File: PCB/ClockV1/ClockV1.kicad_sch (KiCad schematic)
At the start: 41 parts, among them J1 Conn_01x02, J2 Conn_01x02, J3 Conn_01x08, J4 Conn_01x02, Q1 FDN327N, Q2 DMP2045UQ-7, U1 MT3608, U2 MAX14611ETD_, U3 DFR0299, U4 ATtiny1616-M

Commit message: Production to JLCPCB
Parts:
- added H5, H6, H7: MountingHole, MountingHole:ToolingHole_1.152mm, symbol Mechanical:MountingHole
- D2: value BAT43 -> LBAT46T1G
- D3: value LED -> Red; now left out of the parts list
- D4: value LED -> Green; now left out of the parts list
- J1, J2, J3, J4, R6, TP1, TP2, TP3, TP4, TP5, TP6, TP7, U3: now left out of the parts list
- L1: JLCPCB Part # (none) -> C5123081; MANUFACTURER_PART_NUMBER (none) -> SDRH.1209CT.NLF220MT00
- Q2: value DMP2045UQ-7 -> AO3407A; footprint Samacsys:SOT96P240X110-3N -> Package_TO_SOT_SMD:SOT-23-3; Arrow Part Number DMP2045UQ-7 -> (none); Arrow Price/Stock https://www.arrow.com/en/products/dmp2045uq-7/diodes-incorp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 -> (none); JLCPCB Part # (none) -> C5224209; Manufacturer_Name Diodes Incorporated -> ElecSuper; Manufacturer_Part_Number DMP2045UQ-7 -> AO3407A; Mouser Part Number 621-DMP2045UQ-7 -> (none); Mouser Price/Stock https://www.mouser.co.uk/ProductDetail/Diodes-Incorporated/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 -> (none)
- R2: value 442k -> 330k
- U2: value MAX14611ETD_ -> MAX14611ETD+T; JLCPCB Part # (none) -> C2677488

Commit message: Add decoupling capacitors and signal selection jumper for MAX14611
- Added decoupling capacitors (C5/100nF and C6/1uF) for the MAX14611 dual power supplies
- Added solder jumper to allow selection between PON and BR signals for microcontroller input
- Renamed net HBR to Net-(JP2-C) to better reflect its function as jumper connection
- Added new HPONBR signal net for level shifter power control
- Updated PCB date to 2025-05-11
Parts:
- added C5: 100nF, Capacitor_SMD:C_0603_1608Metric, symbol Device:C
- added C6: 1uF, Capacitor_SMD:C_0603_1608Metric, symbol Device:C
- added JP2: PON/BR Select, Jumper:SolderJumper-3_P1.3mm_Open_RoundedPad1.0x1.5mm, symbol Jumper:Jumper_3_Open
- TP2: value HBR -> HPONBR
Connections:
- net +1V5: now also C5.1
- net +3V3: now also C6.1
- net BR: now also JP2.1 (A); no longer U2.2 (I/OVL2)
- net GND: now also C5.2, C6.2
- net PON: now also JP2.3 (B)
- net HBR renamed HPONBR
- new net: JP2.2 (C), U2.2 (I/OVL2)
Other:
- moved on the sheet: JP1, TP1, TP2, TP3, TP4, U2

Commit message: Update of PCB ClockV1
- Export Silkscreen in 3D
- Add jumper to select monitoring PON
- Re-order references
- Monitor +3V0 from uC with ADC and a decoupling capactior
- Changed photoresistor footprint (actual part is smaller than expected)
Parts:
- added C7: 100nF, Capacitor_SMD:C_0603_1608Metric, symbol Device:C
- H5, H6, H7: value MountingHole -> ToolingHole
- R6: footprint OptoDevice:R_LDR_5.1x4.3mm_P3.4mm_Vertical -> OptoDevice:R_LDR_4.9x4.2mm_P2.54mm_Vertical
- renumbered C3 to C1, C1 to C3, C6 to C4, C4 to C6, D4 to D2, D2 to D4, Q2 to Q1, Q1 to Q2, R8 to R10, R10 to R8, TP7 to TP1, TP1 to TP3, TP3 to TP4, TP4 to TP5, TP5 to TP7, U4 to U3, U3 to U4
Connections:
- net +3V0: now also U3.8 (PA7), C7.2
- net GND: now also C7.1
- no-connect marks 13 -> 12

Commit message: Add switch to PCB
- Added a single push button switch
- Added RC filter for (pre-)debounce
- Moved tooling hole to place the button
- Removed some silkscreen labels to make room
- Renumbered components depengind on their placement on the PCB
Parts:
- added C8: 100nF, Capacitor_SMD:C_0603_1608Metric, symbol Device:C
- added R10: 100, Resistor_SMD:R_0603_1608Metric, symbol Device:R
- added R11: 10k, Resistor_SMD:R_0603_1608Metric, symbol Device:R
- added SW1: SW_Push, Button_Switch_THT:SW_PUSH_1P1T_6x3.5mm_H4.3_APEM_MJTP1243, symbol Switch:SW_Push
- renumbered C3 to C1, C1 to C2, C2 to C3, D4 to D2, D2 to D3, D3 to D4, H4 to H2, H5 to H3, H7 to H4, H2 to H5, H3 to H7, J4 to J2, J2 to J4, R2 to R1, R6 to R12, R1 to R2, R10 to R3, R7 to R4, R3 to R5, R9 to R6, R4 to R7, R5 to R9, TP4 to TP1, TP5 to TP2, TP7 to TP3, TP3 to TP4, TP2 to TP5, TP1 to TP7
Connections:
- net +3V3: now also R10.1, SW1.2
- net GND: now also R11.2
- net BTN: now reaches U3.10 (PB4)
- net BTN: now also C8.2, R11.1, SW1.1
- new net: C8.1, R10.2
- no-connect marks 12 -> 11
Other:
- moved on the sheet: D3, D4, R6, R8

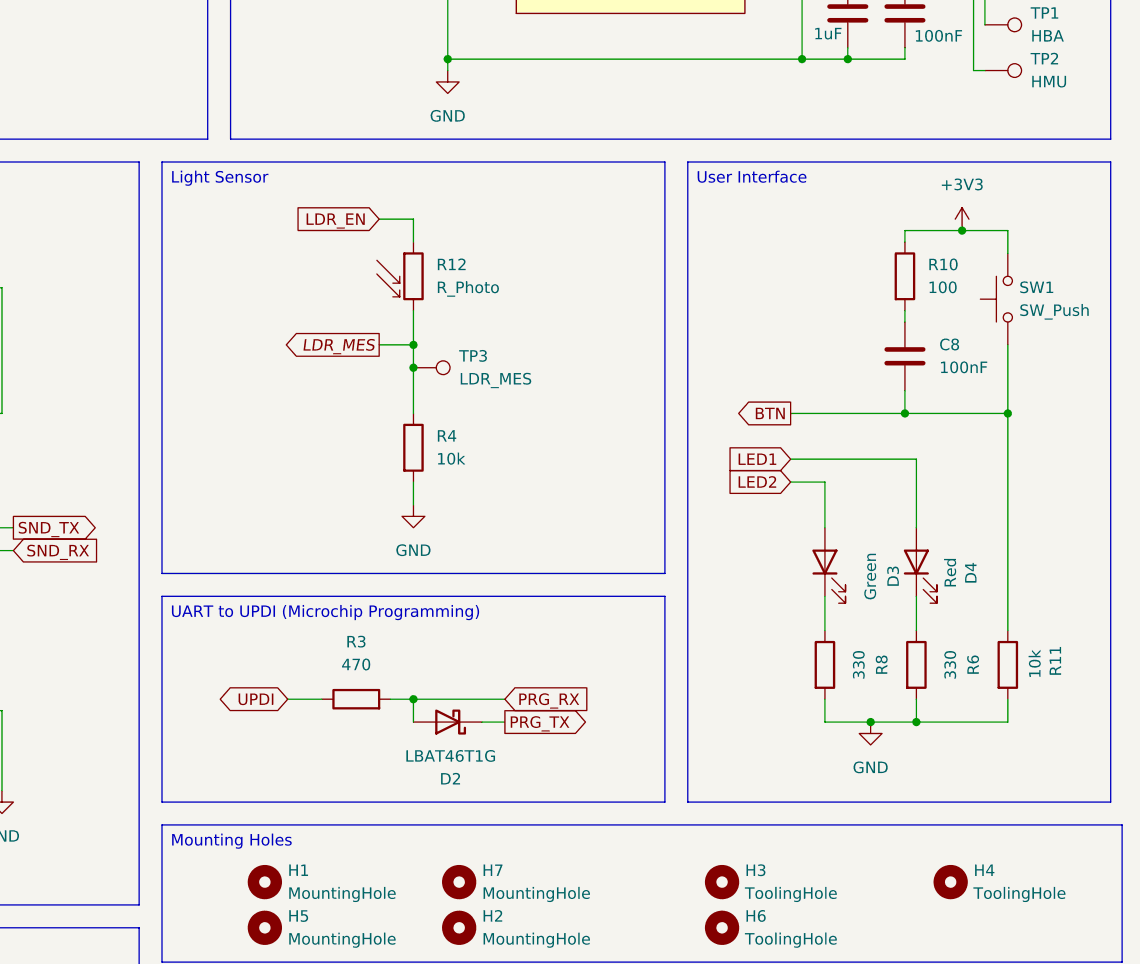
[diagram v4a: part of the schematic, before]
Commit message: Corrected debouncer
- Capacitor was not positionned properly
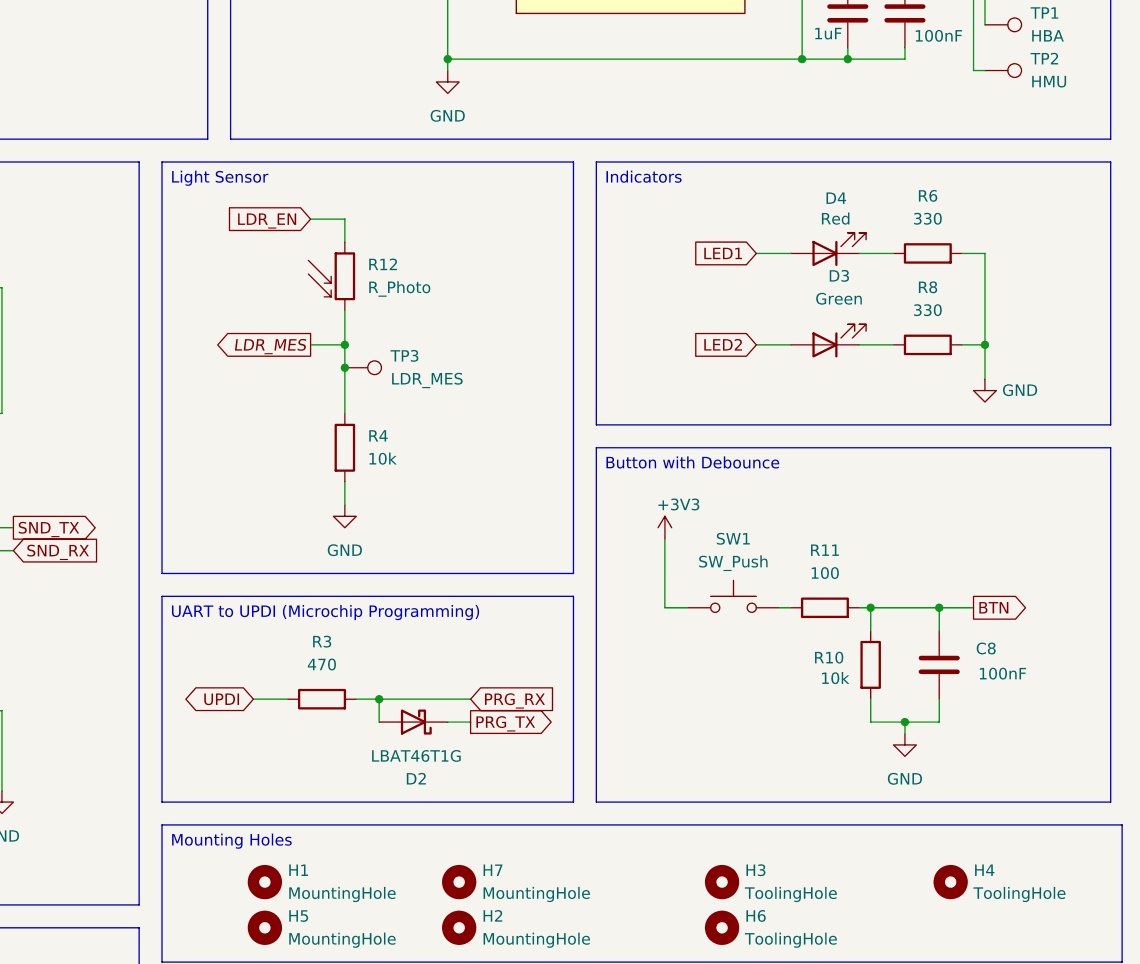
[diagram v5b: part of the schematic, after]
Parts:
- renumbered R11 to R10, R10 to R11
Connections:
- net +3V3: now also SW1.1; no longer R11.1, SW1.2
- net BTN: now also C8.1, R11.2; no longer C8.2, SW1.1
- net GND: now also C8.2
- new net: R11.1, SW1.2
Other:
- moved on the sheet: C8, D2, D3, D4, R10, R11, R12, R3, R4, R6, R8, SW1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

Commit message: Store last changes in ClockV1 before deprecating
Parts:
- SW1: now left out of the parts list
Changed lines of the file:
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@@
+		(polyline
+			(pts
+				(xy 181.61 101.6) (xy 212.09 101.6) (xy 212.09 91.44) (xy 181.61 91.44)
+			)
+			(stroke
+				(width 0)
+				(type dash)
+			)
+			(fill
+				(type none)
+			)
+		)
+	)
+	(rule_area
 		(polyline
 			(pts
@@
 				(type dash)
 				(color 255 153 0 1)
-			)
-			(fill
-				(type none)
-			)
-		)
-	)
-	(rule_area
-		(polyline
-			(pts
-				(xy 181.61 101.6) (xy 212.09 101.6) (xy 212.09 91.44) (xy 181.61 91.44)
-			)
-			(stroke
-				(width 0)
-				(type dash)
 			)
 			(fill
@@
 		(unit 1)
 		(exclude_from_sim no)
-		(in_bom yes)
+		(in_bom no)
 		(on_board yes)
 		(dnp no)
